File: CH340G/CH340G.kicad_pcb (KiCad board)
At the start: 2 copper layers, 25.4 x 15.5 mm, 19 parts, among them J1 USB_B_Micro, J2 Conn_01x06, U1 CH340G, Y1 Crystal

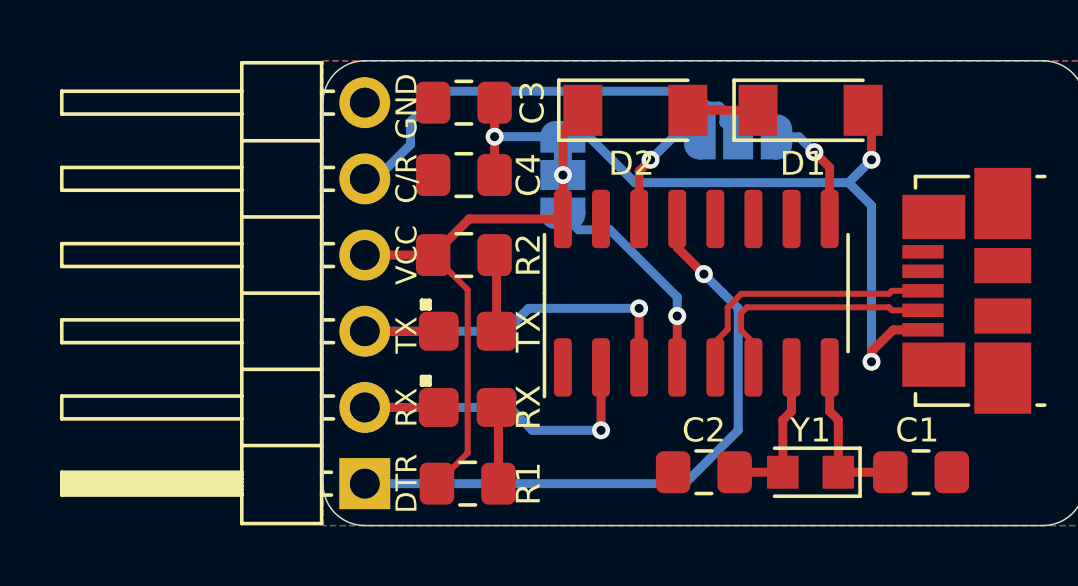
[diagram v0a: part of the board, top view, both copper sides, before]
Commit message: Silkscreen Updates
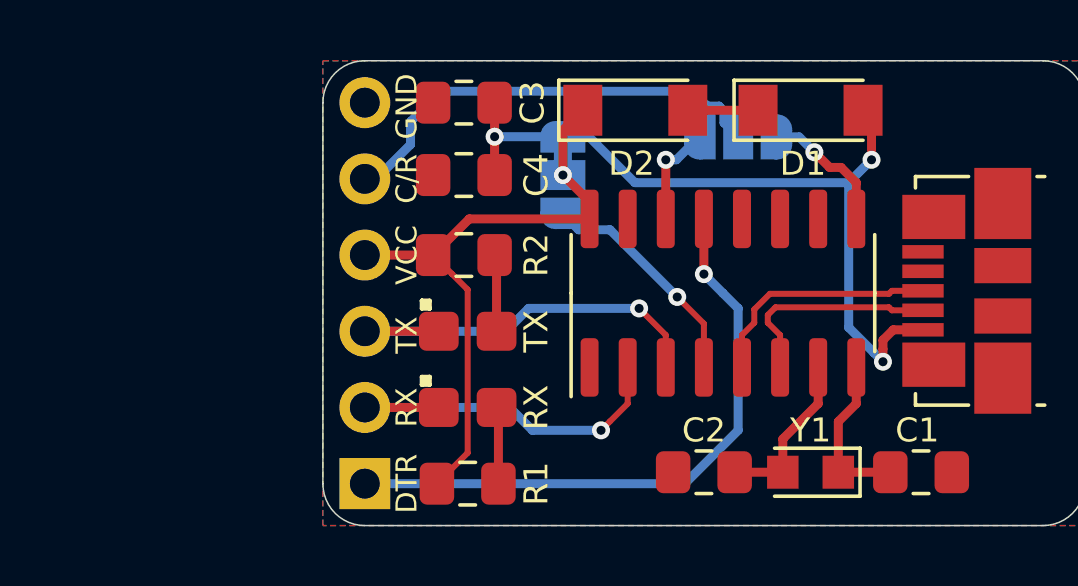
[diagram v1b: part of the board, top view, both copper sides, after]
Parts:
- J2: footprint Connector_PinHeader_2.54mm:PinHeader_1x06_P2.54mm_Horizontal -> Connector_PinHeader_2.54mm:PinHeader_1x06_P2.54mm_Vertical; moved to B.Cu
- moved U1 0.89 mm to (144.0, 95.2)
- turned J2 to 0 degrees
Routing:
- net /5V: track 19.5 -> 20.8 mm
- net /D-: track 8.16 -> 7.24 mm
- net /D+: track 8.91 -> 7.98 mm
- net /RTS: track 4.06 -> 3.40 mm
- net /CTS: track 3.88 -> 4.48 mm
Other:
- board text added: "CH340G USB - UART"
- board text removed: "UART to USB"

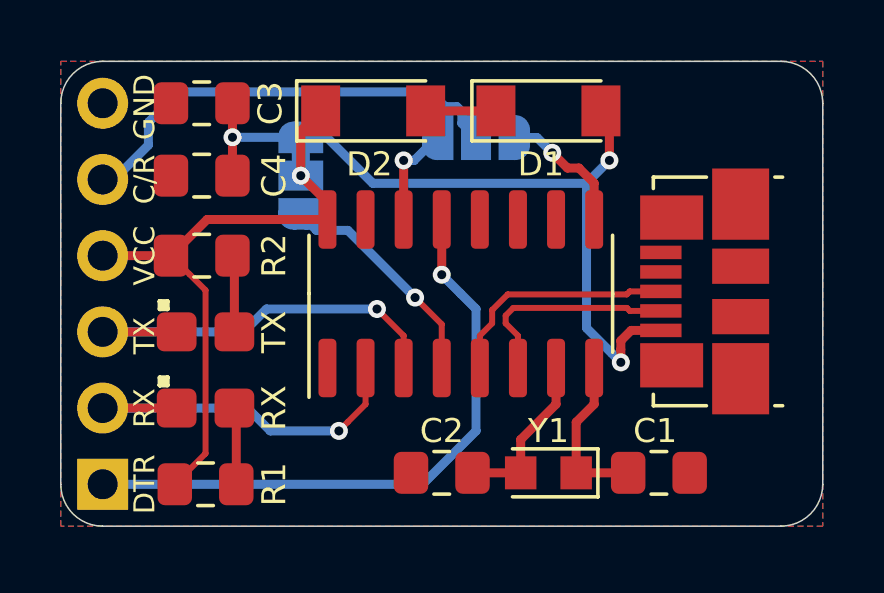
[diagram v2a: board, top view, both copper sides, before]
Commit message: Power LED Added
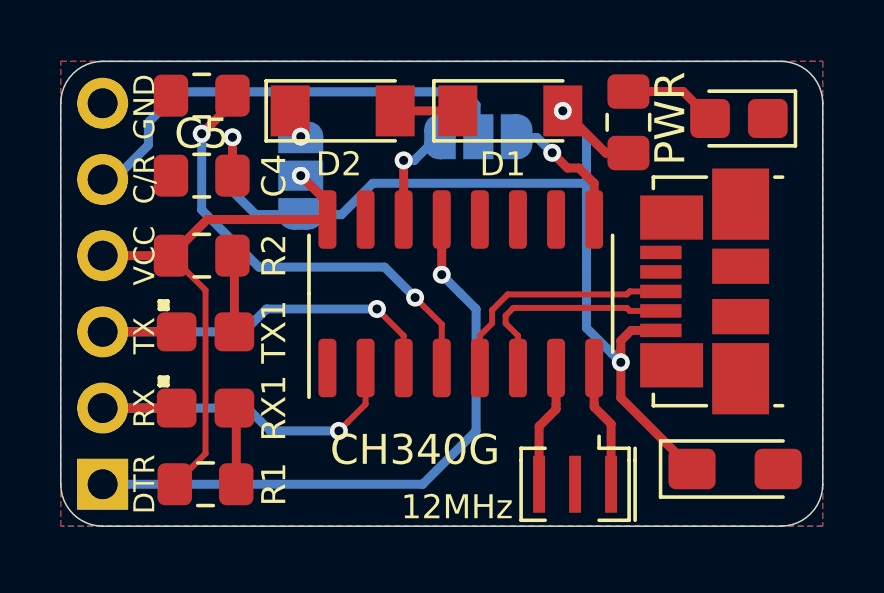
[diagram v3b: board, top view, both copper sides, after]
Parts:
- removed C/R: SolderJumper_3_Bridged12, Jumper:SolderJumper-3_P1.3mm_Open_RoundedPad1.0x1.5mm
- removed C1, C2: 22pF, Capacitor_SMD:C_0805_2012Metric_Pad1.15x1.40mm_HandSolder
- removed Vin: SolderJumper_3_Bridged12, Jumper:SolderJumper-3_P1.3mm_Bridged12_RoundedPad1.0x1.5mm_NumberLabels
- removed Y1: Crystal, Crystal:Crystal_SMD_2012-2Pin_2.0x1.2mm_HandSoldering
- added 12MHz: Resonator, Crystal:Resonator_SMD_muRata_CSTxExxV-3Pin_3.0x1.1mm, F.Cu at (147.8, 101.6)
- added C5: 10nF, Capacitor_SMD:C_0805_2012Metric_Pad1.15x1.40mm_HandSolder, F.Cu at (135.4, 88.6)
- added JP1: SolderJumper_3_Open, Jumper:SolderJumper-3_P1.3mm_Open_RoundedPad1.0x1.5mm, B.Cu at (138.7, 91.3)
- added JP2: SolderJumper_3_Open, Jumper:SolderJumper-3_P1.3mm_Open_RoundedPad1.0x1.5mm, B.Cu at (144.6, 90.0)
- added PWR: LED, LED_SMD:LED_0805_2012Metric_Castellated, F.Cu at (153.3, 89.4)
- added R3: R_US, Resistor_SMD:R_0805_2012Metric_Pad1.15x1.40mm_HandSolder, F.Cu at (149.6, 89.5)
- C3: value 10uF -> 22uF; footprint Capacitor_SMD:C_0805_2012Metric_Pad1.15x1.40mm_HandSolder -> Capacitor_Tantalum_SMD:CP_EIA-3216-18_Kemet-A_Pad1.58x1.35mm_HandSolder
- moved C3 21.6 mm to (153.2, 101.1), turned to 0 degrees
- moved D1 1.27 mm to (145.7, 89.2)
- moved D2 1.02 mm to (140.1, 89.2)
- renumbered U1 to CH340G, RX to RX1, TX to TX1
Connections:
- net Net-(C3-Pad1) renamed /VBUS
- D2 pad 1: /5V -> Net-(D2-Pad1)
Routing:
- net /VBUS: track 26.4 -> 34.7 mm
- net Net-(C5-Pad2): track 7.67 -> 15.3 mm, vias 1 -> 2
- net Net-(PWR1-Pad2): track 0.00 -> 3.09 mm
- net /5V: track 20.8 -> 18.3 mm
- net Net-(U1-Pad7): track 5.59 -> 3.35 mm
- net Net-(U1-Pad8): track 5.48 -> 3.35 mm
- net Net-(D2-Pad1): track 0.00 -> 1.01 mm, vias 0 -> 1
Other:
- board text added: "3V"
- board text added: "5V"
- board text added: "CTS"
- board text added: "RTS"

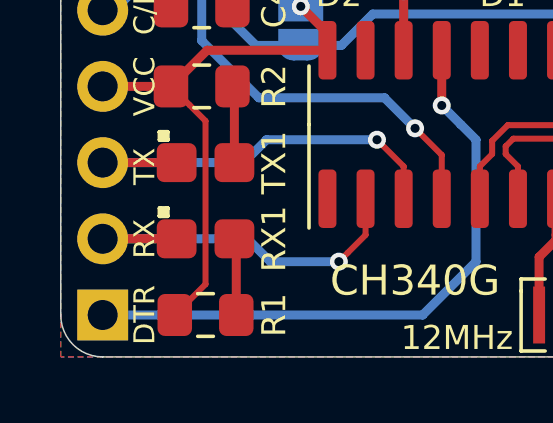
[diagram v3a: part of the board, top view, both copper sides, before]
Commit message: Silkscreen Edits
Dimensions moved to Drawings Layer
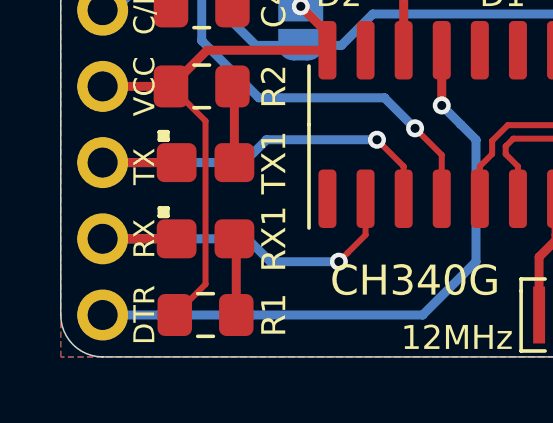
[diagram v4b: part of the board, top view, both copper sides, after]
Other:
- rule pad_to_mask_clearance: 0.051 -> 0
- rule solder_mask_min_width: 0.25 -> 0.1
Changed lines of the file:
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@@
   )
   (setup
-    (last_trace_width 0.3)
+    (last_trace_width 0.127)
     (user_trace_width 0.15)
     (user_trace_width 0.2)
@@
     (mod_text_size 1 1)
     (mod_text_width 0.15)
-    (pad_size 1.524 1.524)
-    (pad_drill 0.762)
-    (pad_to_mask_clearance 0.051)
-    (solder_mask_min_width 0.25)
+    (pad_size 1.7 1.7)
+    (pad_drill 1)
+    (pad_to_mask_clearance 0)
+    (solder_mask_min_width 0.1)
     (aux_axis_origin 0 0)
     (visible_elements 7FFFFFFF)
     (pcbplotparams
-      (layerselection 0x010fc_ffffffff)
+      (layerselection 0x010f0_ffffffff)
       (usegerberextensions false)
       (usegerberattributes false)
@@
       (viasonmask false)
       (mode 1)
-      (useauxorigin false)
+      (useauxorigin true)
       (hpglpennumber 1)
       (hpglpenspeed 20)
@@
       (psa4output false)
       (plotreference true)
-      (plotvalue true)
+      (plotvalue false)
       (plotinvisibletext false)
       (padsonsilk false)
@@
       (outputformat 1)
       (mirror false)
-      (drillshape 1)
+      (drillshape 0)
       (scaleselection 1)
-      (outputdirectory ""))
+      (outputdirectory "../../Gerbers/CH340G/"))
   )
   (net 0 "")
@@
     (pad 2 thru_hole oval (at 0 -2.54) (size 1.7 1.7) (drill 1) (layers *.Cu *.Mask)
       (net 4 /RX))
-    (pad 1 thru_hole rect (at 0 0) (size 1.7 1.7) (drill 1) (layers *.Cu *.Mask)
+    (pad 1 thru_hole circle (at 0 0) (size 1.7 1.7) (drill 1) (layers *.Cu *.Mask)
       (net 10 /DTR))
     (model ${KISYS3DMOD}/Connector_PinHeader_2.54mm.3dshapes/PinHeader_1x06_P2.54mm_Vertical.wrl
@@
   (gr_arc (start 132.08 101.6) (end 130.683 101.6) (angle -90) (layer Edge.Cuts) (width 0.05))
   (gr_arc (start 132.08 88.9) (end 132.08 87.503) (angle -90) (layer Edge.Cuts) (width 0.05))
-  (segment (start 136.407 90.034) (end 136.407 91.313) (width 0.3) (layer F.Cu) (net 20))
-  (via (at 136.407 90.034) (size 0.6) (drill 0.3) (layers F.Cu B.Cu) (net 20))
-  (segment (start 141.085592 91.567) (end 148.209 91.567) (width 0.3) (layer B.Cu) (net 20))
-  (via (at 149.352 97.536) (size 0.6) (drill 0.3) (layers F.Cu B.Cu) (net 20))
-  (segment (start 149.052001 97.236001) (end 149.352 97.536) (width 0.3) (layer B.Cu) (net 20))
-  (segment (start 148.209 91.567) (end 148.209 96.393) (width 0.3) (layer B.Cu) (net 20))
-  (segment (start 149.352 97.111736) (end 149.352 97.536) (width 0.3) (layer F.Cu) (net 20))
-  (segment (start 149.352 96.816) (end 149.352 97.111736) (width 0.3) (layer F.Cu) (net 20))
-  (segment (start 149.696 96.472) (end 149.352 96.816) (width 0.3) (layer F.Cu) (net 20))
-  (segment (start 150.686 96.472) (end 149.696 96.472) (width 0.3) (layer F.Cu) (net 20))
-  (segment (start 148.209 96.393) (end 149.052001 97.236001) (width 0.3) (layer B.Cu) (net 20))
   (segment (start 141.859 89.154) (end 144.201 89.154) (width 0.3) (layer F.Cu) (net 2))
   (segment (start 132.08 93.98) (end 134.357 93.98) (width 0.3) (layer F.Cu) (net 3))
@@
   (segment (start 134.357 93.98) (end 135.562 92.775) (width 0.3) (layer F.Cu) (net 3))
   (segment (start 135.562 92.775) (end 139.573 92.775) (width 0.3) (layer F.Cu) (net 3))
-  (segment (start 136.534 99.1225) (end 136.4715 99.06) (width 0.3) (layer F.Cu) (net 18))
-  (segment (start 136.534 101.6) (end 136.534 99.1225) (width 0.3) (layer F.Cu) (net 18))
   (segment (start 134.5465 99.06) (end 132.08 99.06) (width 0.3) (layer F.Cu) (net 4))
   (segment (start 132.08 99.06) (end 136.906 99.06) (width 0.3) (layer B.Cu) (net 4))
@@
   (segment (start 140.843 97.725) (end 140.843 98.933) (width 0.2) (layer F.Cu) (net 4))
   (segment (start 140.843 98.933) (end 140.253999 99.522001) (width 0.2) (layer F.Cu) (net 4))
-  (segment (start 136.4715 94.0445) (end 136.407 93.98) (width 0.3) (layer F.Cu) (net 19))
-  (segment (start 136.4715 96.52) (end 136.4715 94.0445) (width 0.3) (layer F.Cu) (net 19))
   (segment (start 134.5465 96.52) (end 132.08 96.52) (width 0.3) (layer F.Cu) (net 5))
   (segment (start 132.08 96.52) (end 136.779 96.52) (width 0.3) (layer B.Cu) (net 5))
@@
   (segment (start 143.383 94.614998) (end 143.382998 94.615) (width 0.3) (layer F.Cu) (net 10))
   (segment (start 143.383 92.775) (end 143.383 94.614998) (width 0.3) (layer F.Cu) (net 10))
-  (via (at 142.494 95.377) (size 0.6) (drill 0.3) (layers F.Cu B.Cu) (net 21))
-  (segment (start 143.383 96.266) (end 142.494 95.377) (width 0.2) (layer F.Cu) (net 21))
-  (segment (start 143.383 97.725) (end 143.383 96.266) (width 0.2) (layer F.Cu) (net 21))
   (via (at 147.066 90.551) (size 0.6) (drill 0.3) (layers F.Cu B.Cu) (net 11))
   (segment (start 146.558 90.043) (end 147.066 90.551) (width 0.3) (layer B.Cu) (net 11))
@@
   (segment (start 151.4285 88.51) (end 149.606 88.51) (width 0.3) (layer F.Cu) (net 17))
   (segment (start 152.3265 89.408) (end 151.4285 88.51) (width 0.3) (layer F.Cu) (net 17))
+  (segment (start 136.534 99.1225) (end 136.4715 99.06) (width 0.3) (layer F.Cu) (net 18))
+  (segment (start 136.534 101.6) (end 136.534 99.1225) (width 0.3) (layer F.Cu) (net 18))
+  (segment (start 136.4715 94.0445) (end 136.407 93.98) (width 0.3) (layer F.Cu) (net 19))
+  (segment (start 136.4715 96.52) (end 136.4715 94.0445) (width 0.3) (layer F.Cu) (net 19))
+  (segment (start 136.407 90.034) (end 136.407 91.313) (width 0.3) (layer F.Cu) (net 20))
+  (via (at 136.407 90.034) (size 0.6) (drill 0.3) (layers F.Cu B.Cu) (net 20))
+  (segment (start 141.085592 91.567) (end 148.209 91.567) (width 0.3) (layer B.Cu) (net 20))
+  (via (at 149.352 97.536) (size 0.6) (drill 0.3) (layers F.Cu B.Cu) (net 20))
+  (segment (start 149.052001 97.236001) (end 149.352 97.536) (width 0.3) (layer B.Cu) (net 20))
+  (segment (start 148.209 91.567) (end 148.209 96.393) (width 0.3) (layer B.Cu) (net 20))
+  (segment (start 149.352 97.111736) (end 149.352 97.536) (width 0.3) (layer F.Cu) (net 20))
+  (segment (start 149.352 96.816) (end 149.352 97.111736) (width 0.3) (layer F.Cu) (net 20))
+  (segment (start 149.696 96.472) (end 149.352 96.816) (width 0.3) (layer F.Cu) (net 20))
+  (segment (start 150.686 96.472) (end 149.696 96.472) (width 0.3) (layer F.Cu) (net 20))
+  (segment (start 148.209 96.393) (end 149.052001 97.236001) (width 0.3) (layer B.Cu) (net 20))
   (segment (start 149.352 98.7195) (end 151.7245 101.092) (width 0.3) (layer F.Cu) (net 20))
   (segment (start 149.352 97.536) (end 149.352 98.7195) (width 0.3) (layer F.Cu) (net 20))
@@
   (segment (start 147.419005 89.154005) (end 147.447005 89.154005) (width 0.3) (layer F.Cu) (net 20))
   (segment (start 147.447005 89.154005) (end 148.853 90.56) (width 0.3) (layer F.Cu) (net 20))
+  (via (at 142.494 95.377) (size 0.6) (drill 0.3) (layers F.Cu B.Cu) (net 21))
+  (segment (start 143.383 96.266) (end 142.494 95.377) (width 0.2) (layer F.Cu) (net 21))
+  (segment (start 143.383 97.725) (end 143.383 96.266) (width 0.2) (layer F.Cu) (net 21))
   (via (at 135.382 89.916) (size 0.6) (drill 0.3) (layers F.Cu B.Cu) (net 21))
   (segment (start 136.407 88.646) (end 136.407 88.891) (width 0.3) (layer F.Cu) (net 21))

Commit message: Page Settings Updated
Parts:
- moved C4 87.9 mm to (61.5, 43.8)
- moved D1 87.9 mm to (71.8, 41.7)
- moved G*** 87.9 mm to (70.6, 51.1)
- moved J2 87.9 mm to (58.2, 54.1)
- moved JP1 87.9 mm to (64.8, 43.8)
- moved JP2 87.9 mm to (70.7, 42.5)
- moved R2 87.9 mm to (61.5, 46.5)
- moved 12MHz 87.9 mm to (73.9, 54.1)
- moved C3 87.9 mm to (79.2, 53.6)
- moved C5 87.9 mm to (61.5, 41.1)
- moved CH340G 87.9 mm to (70.1, 47.8)
- moved D2 87.9 mm to (66.2, 41.7)
- moved G*** 87.9 mm to (63.5, 51.1)
- moved G*** 87.9 mm to (79.5, 47.8)
- moved J1 87.9 mm to (78.2, 47.7)
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
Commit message: CH340G Revision 2
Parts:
- removed 12MHz: Resonator, Crystal:Resonator_SMD_muRata_CSTxExxV-3Pin_3.0x1.1mm
- removed CH340G: CH340G, Package_SO:SOIC-16_3.9x9.9mm_P1.27mm
- removed D2: D, Diode_SMD:D_MiniMELF
- removed J1: USB_B_Micro, Connector_USB:USB_Micro-B_Molex_47346-0001
- removed JP1, JP2: SolderJumper_3_Open, Jumper:SolderJumper-3_P1.3mm_Open_RoundedPad1.0x1.5mm
- removed the PWR at (79.4, 41.9)
- removed TX1: LED, LED_SMD:LED_0805_2012Metric_Castellated
- added C1: 9pF, Capacitor_SMD:C_0603_1608Metric, F.Cu at (67.8, 38.4)
- added C2: 9pF, Capacitor_SMD:C_0603_1608Metric, F.Cu at (64.4, 41.0)
- added C6: 10uF, Capacitor_SMD:C_0805_2012Metric, F.Cu at (64.4, 42.9)
- added C7: 10uF, Capacitor_SMD:C_0805_2012Metric, F.Cu at (64.4, 48.1)
- added F1: 500mA, Resistor_SMD:R_0805_2012Metric, F.Cu at (64.0, 34.7)
- added P1: USB_C_Plug_USB2.0, SirBoardLibrary:USB_C, F.Cu at (73.5, 35.8)
- added PWR: BLUE, LED_SMD:LED_0603_1608Metric, F.Cu at (76.8, 33.9)
- added Pin 6: SolderJumper_3_Open, Jumper:SolderJumper-3_P1.3mm_Open_RoundedPad1.0x1.5mm, B.Cu at (70.4, 46.4)
- added TX2: RED, LED_SMD:LED_0603_1608Metric, F.Cu at (70.5, 48.4)
- added U1: CH340G, Package_SO:SOIC-16_3.9x9.9mm_P1.27mm, F.Cu at (71.9, 43.7)
- added U2: AP2127K-3.3, Package_TO_SOT_SMD:SOT-23-5, F.Cu at (64.6, 45.5)
- added VCC: SolderJumper_3_Open, Jumper:SolderJumper-3_P1.3mm_Open_RoundedPad1.0x1.5mm, B.Cu at (70.4, 42.2)
- added Y1: Crystal_GND24, Crystal:Crystal_SMD_SeikoEpson_TSX3225-4Pin_3.2x2.5mm, F.Cu at (64.9, 38.4)
- C4, C5: footprint Capacitor_SMD:C_0805_2012Metric_Pad1.15x1.40mm_HandSolder -> Capacitor_SMD:C_0603_1608Metric
- D1: value D -> PRTR5V0U2X; footprint Diode_SMD:D_MiniMELF -> SirBoardLibrary:SOT-143
- G***: footprint logo:SirUSB76x29 -> logo:SirUSB66x25
- G***: footprint logo:SirBoard112x35 -> logo:SirBoard98x31
- G***: footprint logo:logo94x134 -> logo:logo76x107
- R1, R2, R3: value R_US -> 1K; footprint Resistor_SMD:R_0805_2012Metric_Pad1.15x1.40mm_HandSolder -> Resistor_SMD:R_0603_1608Metric
- RX1: value LED -> GREEN; footprint LED_SMD:LED_0805_2012Metric_Castellated -> LED_SMD:LED_0603_1608Metric
- moved R1 28.6 mm to (76.8, 29.8), turned to 270 degrees
- moved C3 27.5 mm to (64.3, 30.5), turned to 90 degrees
- moved G*** 19.0 mm to (70.4, 32.0), turned to 180 degrees
- moved J2 18.7 mm to (76.7, 51.7), turned to 90 degrees
- moved C4 15.2 mm to (75.6, 38.1), turned to 270 degrees
- moved G*** 14.3 mm to (76.5, 45.0), turned to 270 degrees
- moved G*** 13.6 mm to (70.4, 37.7), turned to 180 degrees
- moved C5 12.8 mm to (73.9, 38.1), turned to 270 degrees
- moved RX1 12.5 mm to (73.7, 48.4)
- moved R3 6.40 mm to (76.5, 48.4), turned to 180 degrees
- moved R2 6.36 mm to (67.5, 48.4)
- moved D1 3.74 mm to (70.6, 38.1), turned to 90 degrees
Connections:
- C3 pad 1: /VBUS -> VBUS
- C3 pad 2: /GND -> GND
- C4 pad 1: /VBUS -> VBUS
- C4 pad 2: /GND -> GND
- C5 pad 1: /GND -> GND
- C5 pad 2: Net-(C5-Pad2) -> 3V3
- D1 pad 1: Net-(D1-Pad1) -> GND
- D1 pad 2: /VBUS -> D+
- J2 pad 1: /DTR -> P6
- J2 pad 2: /RX -> RX
- J2 pad 3: /TX -> TX
- J2 pad 4: /5V -> VCC
- J2 pad 5: /R_C -> CTS
- J2 pad 6: /GND -> GND
- R1 pad 1: /5V -> VCC
- R1 pad 2: Net-(R1-Pad2) -> Net-(PWR1-Pad2)
- R2 pad 1: /5V -> TX
- R3 pad 1: /VBUS -> RX
- R3 pad 2: Net-(PWR1-Pad2) -> Net-(R3-Pad2)
- RX1 pad 1: /RX -> GND
- RX1 pad 2: Net-(R1-Pad2) -> Net-(R3-Pad2)
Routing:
- net VCC: track 0.00 -> 43.6 mm, vias 0 -> 5
- net /VBUS: track 34.7 -> 0.00 mm, vias 3 -> 0
- net VBUS: track 0.00 -> 33.0 mm, vias 0 -> 4
- net /DTR: track 20.4 -> 0.00 mm, vias 1 -> 0
- net TX: track 0.00 -> 19.7 mm, vias 0 -> 1
- net 3V3: track 0.00 -> 18.5 mm, vias 0 -> 2
- net /5V: track 18.3 -> 0.00 mm, vias 1 -> 0
- net RX: track 0.00 -> 15.9 mm, vias 0 -> 2
- net /R_C: track 15.4 -> 0.00 mm
- net Net-(C5-Pad2): track 15.3 -> 0.00 mm, vias 2 -> 0
- net /TX: track 14.3 -> 0.00 mm, vias 1 -> 0
- net Net-(F1-Pad2): track 0.00 -> 13.4 mm, vias 0 -> 2
- net /RX: track 13.1 -> 0.00 mm, vias 1 -> 0
- net D-: track 0.00 -> 11.9 mm
- net D+: track 0.00 -> 11.8 mm, vias 0 -> 2
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- added copper zone on B.Cu, net 3V3
- added copper zone on F.Cu, net GND
- removed copper zone on B.Cu, net /GND
- removed copper zone on F.Cu, net /GND
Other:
- board size 25.4 x 15.5 mm -> 15.5 x 25.4 mm
- board text added: "3V3"
- board text removed: "3V"
- board text removed: "C/R"
